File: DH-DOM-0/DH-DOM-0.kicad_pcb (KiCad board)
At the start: 2 copper layers, 40 x 40 mm, 45 parts, among them J1 USB_C_Receptacle_USB2.0_14P, J2 Conn_01x02, Q1 FDN340P, SW1 RST, SW2 BOOT, U2 MMC5983MA, U4 NCP1117-3.3_SOT223, U5 TVS1400DRV, U6 ESP32-S3-WROOM-1-N4R8, U7 TP4057, U8 ST7789, U9 LSM6DSV16BTR

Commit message: edit
git push sum idk rlly
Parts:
- added C3: 100n, Capacitor_SMD:C_0805_2012Metric, B.Cu at (143.0, 103.0)
- renumbered C9 to C10, C10 to C11, C11 to C12, C12 to C13, C13 to C14, C3 to C4, C4 to C5, C5 to C6, C6 to C7, C7 to C8, C8 to C9, U9 to U1, U2 to U3, U4 to U5, U5 to U6, U6 to U7, U7 to U8, U8 to U9
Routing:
- net +3V3: track 133.7 -> 142.5 mm, vias 8 -> 9

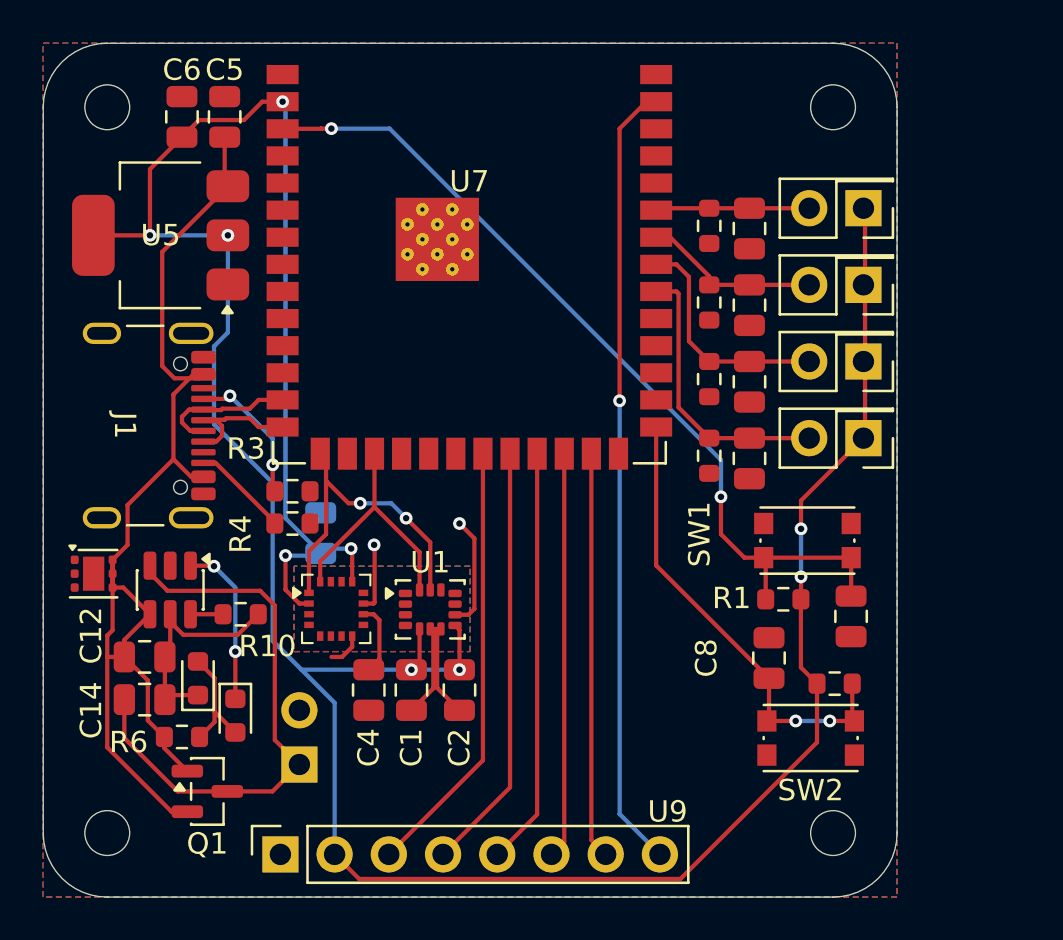
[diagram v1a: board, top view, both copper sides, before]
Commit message: edit
put everything on top layer 3v3 cap
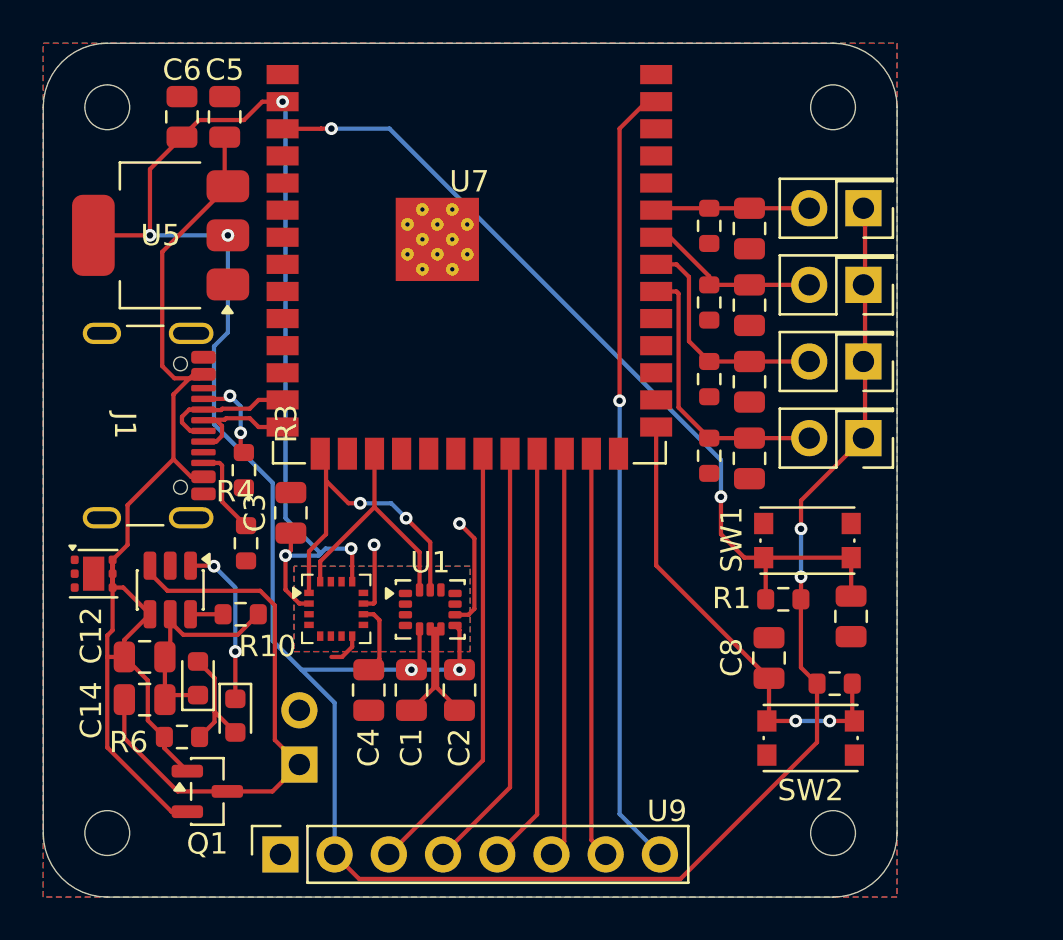
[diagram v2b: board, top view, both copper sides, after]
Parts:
- C3: moved to F.Cu
- moved R3 2.48 mm to (139.4, 100.0), turned to -90 degrees
- moved R4 2.36 mm to (139.5, 103.4), turned to -90 degrees
- moved C3 1.69 mm to (141.6, 102.0)
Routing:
- net Net-(J1-CC1): track 6.64 -> 4.23 mm
- net +3V3: track 142.5 -> 143.7 mm

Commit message: edit
new header pitch
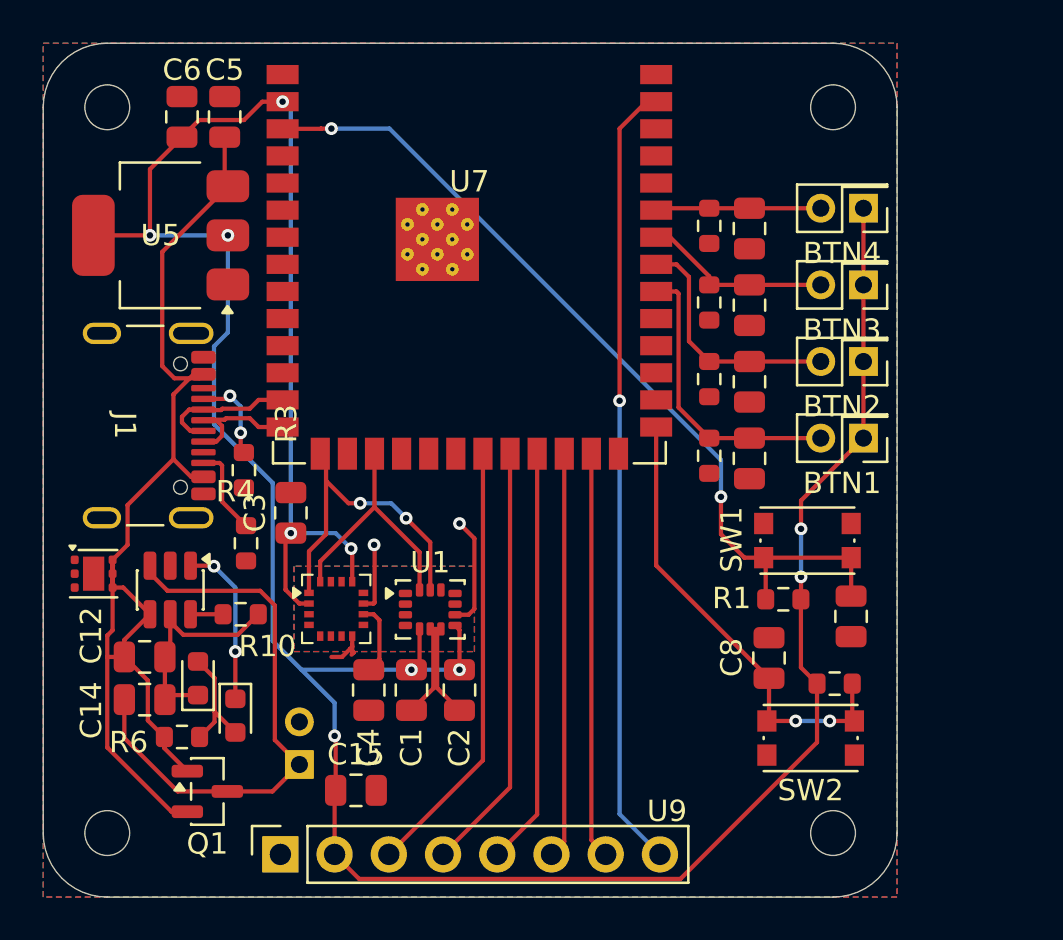
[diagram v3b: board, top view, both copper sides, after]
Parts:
- added C15: 100n, Capacitor_SMD:C_0805_2012Metric, F.Cu at (144.7, 115.0)
- BTN1, BTN2, BTN3, BTN4, J2: footprint Connector_PinHeader_2.54mm:PinHeader_2x01_P2.54mm_Vertical -> Connector_PinHeader_2.00mm:PinHeader_2x01_P2.00mm_Vertical
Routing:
- net +3V3: track 143.7 -> 142.1 mm, vias 9 -> 10
- net GND: track 19.4 -> 20.0 mm

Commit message: edit
dont know either
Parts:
- BTN1, BTN2, BTN3, BTN4: footprint Connector_PinHeader_2.00mm:PinHeader_2x01_P2.00mm_Vertical -> Connector_PinHeader_2.00mm:PinHeader_2x01_P2.00mm_Horizontal
- moved BTN4 2.03 mm to (166.4, 87.7), turned to 0 degrees
- moved BTN3 2.00 mm to (166.4, 91.3), turned to 0 degrees
- moved BTN1 2.00 mm to (166.4, 98.5), turned to 0 degrees
- moved BTN2 2.00 mm to (166.4, 94.9), turned to 0 degrees
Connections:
- BTN1 pad 1: +3V3 -> /BTN1
- BTN1 pad 2: /BTN1 -> +3V3
- BTN2 pad 1: +3V3 -> /BTN2
- BTN2 pad 2: /BTN2 -> +3V3
- BTN3 pad 1: +3V3 -> /BTN3
- BTN3 pad 2: /BTN3 -> +3V3
- BTN4 pad 1: +3V3 -> /BTN4
- BTN4 pad 2: /BTN4 -> +3V3
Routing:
- net /BTN1: track 13.7 -> 11.8 mm

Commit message: eduiyuyt
durrrrrrrr
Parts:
- removed U1: LSM6DSV16BTR, Package_LGA:LGA-14_3x2.5mm_P0.5mm_LayoutBorder3x4y
- added U4: BMI270, Package_LGA:Bosch_LGA-14_3x2.5mm_P0.5mm, F.Cu at (148.0, 106.6)
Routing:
- net GND: track 20.0 -> 7.77 mm, vias 2 -> 1
- net /BTN1: track 11.8 -> 13.7 mm
